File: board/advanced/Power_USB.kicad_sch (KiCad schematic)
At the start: 19 parts, among them J2 Jack-DC, J3 USB_C_Receptacle_USB2.0_16P, Q1 DMP6050SSD, SW2 SW_Reset, U4 STUSB4500QTR

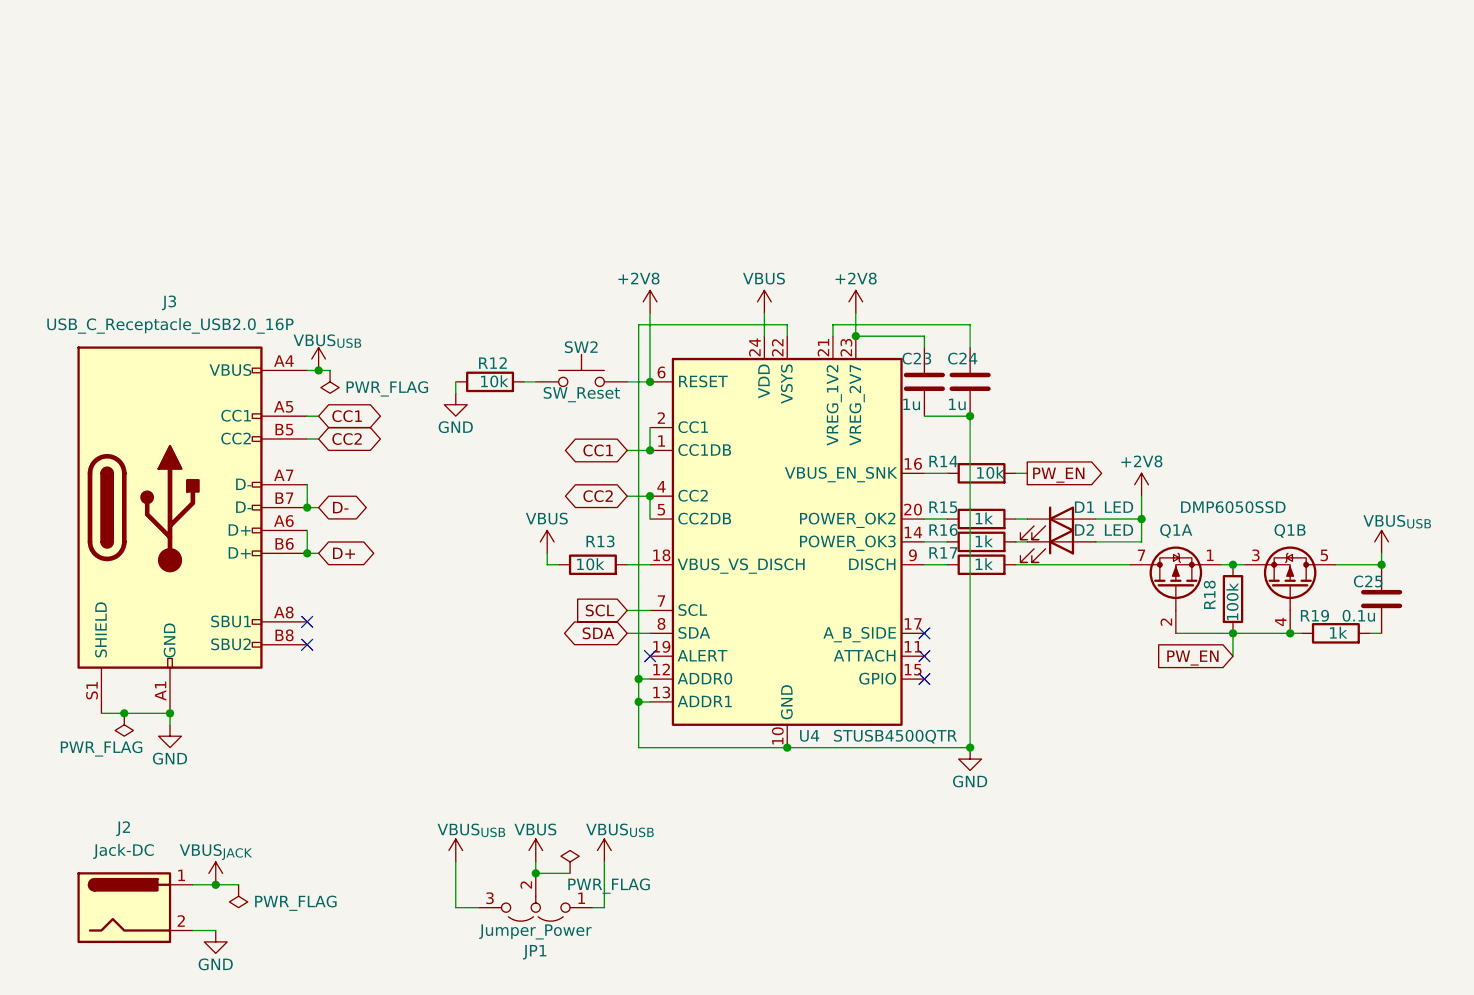
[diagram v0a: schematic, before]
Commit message: put footprints and change schematics
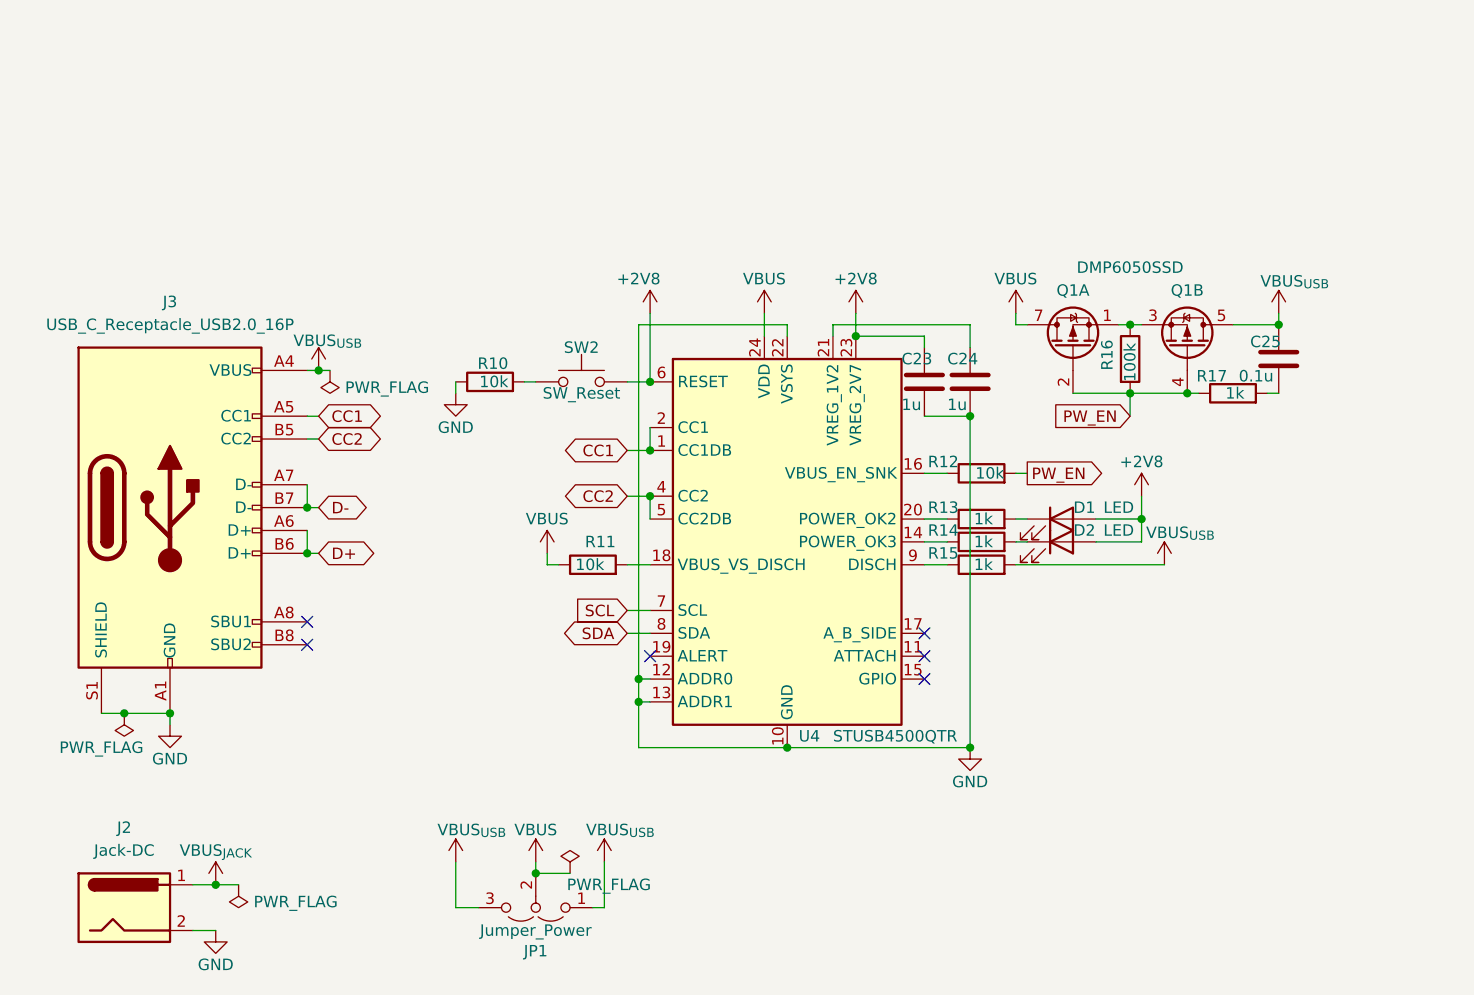
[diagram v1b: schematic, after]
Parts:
- J3: footprint Connector_USB:USB_C_Receptacle_GCT_USB4085 -> NELTRON_5077CR-16SMC2-BK-TR:NELTRON_5077CR-16SMC2-BK-TR
- R10: renamed from R12; footprint Resistor_SMD:R_0603_1608Metric -> Resistor_SMD:R_0402_1005Metric
- R11: renamed from R13; footprint Resistor_SMD:R_0603_1608Metric -> Resistor_SMD:R_0402_1005Metric
- R12: renamed from R14; footprint Resistor_SMD:R_0603_1608Metric -> Resistor_SMD:R_0402_1005Metric
- R13: renamed from R15; footprint Resistor_SMD:R_0603_1608Metric -> Resistor_SMD:R_0402_1005Metric
- R14: renamed from R16; footprint Resistor_SMD:R_0603_1608Metric -> Resistor_SMD:R_0402_1005Metric
- R15: renamed from R17; footprint Resistor_SMD:R_0603_1608Metric -> Resistor_SMD:R_0402_1005Metric
- R16: renamed from R18; footprint Resistor_SMD:R_0603_1608Metric -> Resistor_SMD:R_0402_1005Metric
- R17: renamed from R19; footprint Resistor_SMD:R_0603_1608Metric -> Resistor_SMD:R_0402_1005Metric
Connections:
- net VBUS: now also Q1.7 (D1), Q1.8 (D1)
- net VBUS_{USB}: now also R15.2
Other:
- moved on the sheet: C25, Q1A, Q1B, R16, R17

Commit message: change schematics and complete wiring
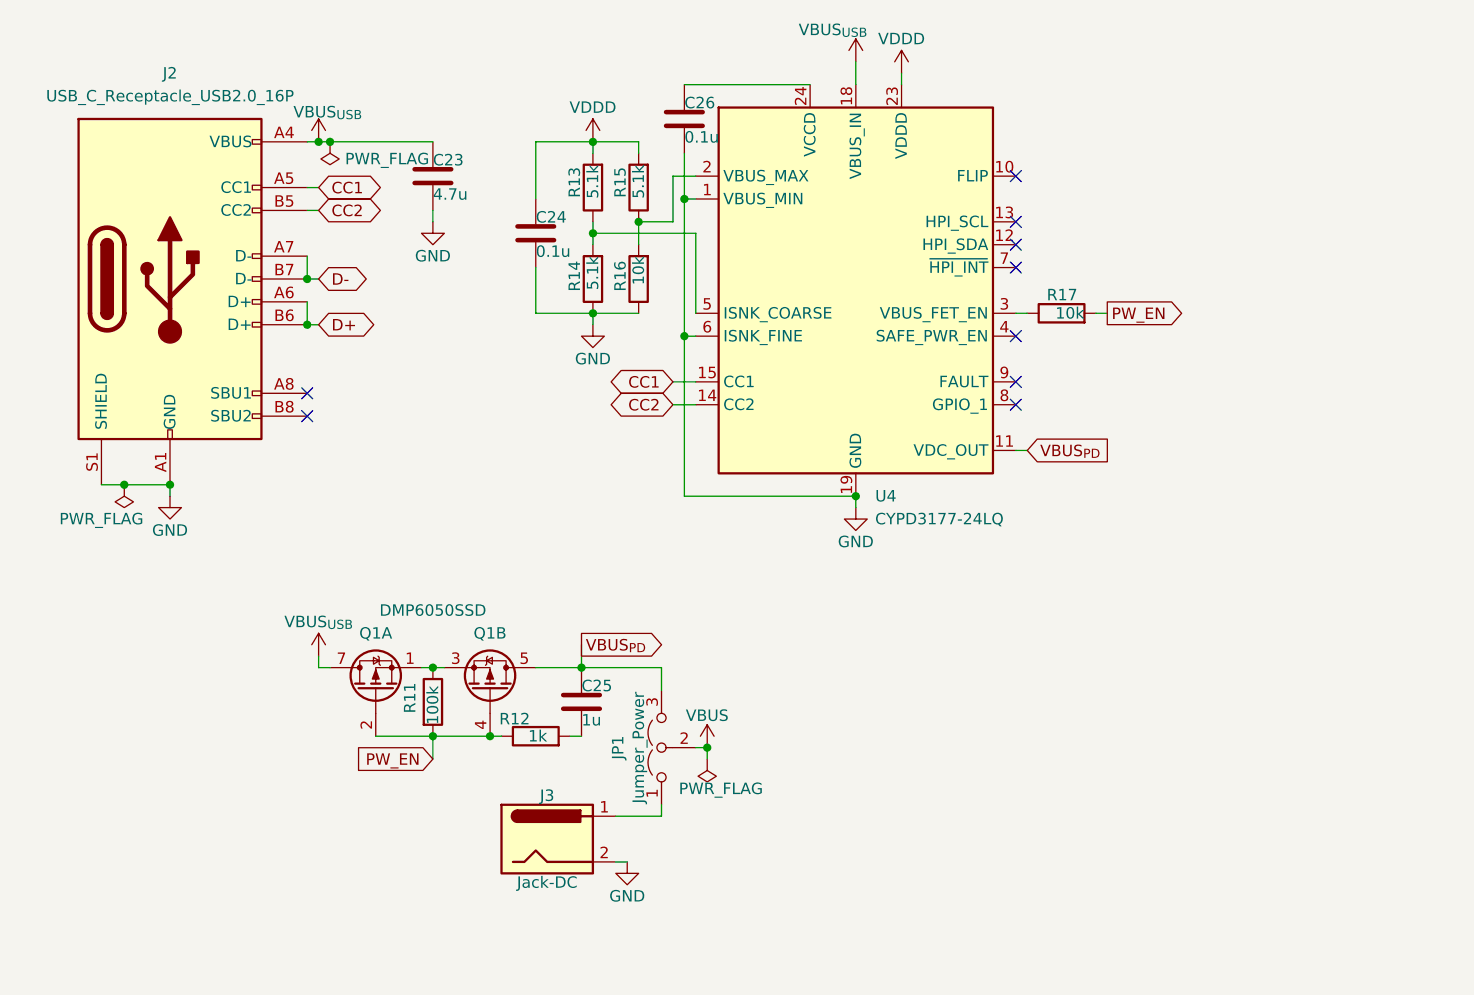
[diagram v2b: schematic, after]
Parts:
- removed D1, D2: LED, LED_SMD:LED_0603_1608Metric, symbol Device:LED
- removed R10, R11: 10k, Resistor_SMD:R_0402_1005Metric, symbol Device:R
- removed SW2: SW_Reset, SW_SKRPACE010:SW_SKRPACE010, symbol Switch:SW_Push
- removed U4: STUSB4500QTR, Package_DFN_QFN:QFN-24-1EP_4x4mm_P0.5mm_EP2.7x2.7mm, symbol Interface_USB:STUSB4500QTR
- added C26: 0.1u, C_0402_1005Metric_small_pads:C_0402_1005Metric_small_pads, symbol Device:C
- added R16: 10k, C_0402_1005Metric_small_pads:C_0402_1005Metric_small_pads, symbol Device:R
- added U4: CYPD3177-24LQ, Package_DFN_QFN:QFN-24-1EP_4x4mm_P0.5mm_EP2.75x2.75mm, symbol Interface_USB:CYPD3177-24LQ
- C23: value 1u -> 4.7u; footprint Capacitor_SMD:C_0201_0603Metric -> C_0402_1005Metric_small_pads:C_0402_1005Metric_small_pads
- C24: value 1u -> 0.1u; footprint Capacitor_SMD:C_0201_0603Metric -> C_0402_1005Metric_small_pads:C_0402_1005Metric_small_pads
- C25: value 0.1u -> 1u; footprint Capacitor_SMD:C_0201_0603Metric -> C_0402_1005Metric_small_pads:C_0402_1005Metric_small_pads
- R11: renamed from R16; footprint Resistor_SMD:R_0402_1005Metric -> C_0402_1005Metric_small_pads:C_0402_1005Metric_small_pads
- R12: renamed from R17; footprint Resistor_SMD:R_0402_1005Metric -> C_0402_1005Metric_small_pads:C_0402_1005Metric_small_pads
- R13, R14, R15: value 1k -> 5.1k; footprint Resistor_SMD:R_0402_1005Metric -> C_0402_1005Metric_small_pads:C_0402_1005Metric_small_pads
- R17: renamed from R12; footprint Resistor_SMD:R_0402_1005Metric -> C_0402_1005Metric_small_pads:C_0402_1005Metric_small_pads
- renumbered J3 to J2, J2 to J3
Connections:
- net +2V8 is gone; now on net VBUS_{USB}: C23.1
- net CC1: now also U4.15 (CC1)
- net CC2: now also U4.14 (CC2)
- net GND: now also R14.1, C26.2, R16.1, U4.1 (VBUS_MIN), U4.19 (GND), U4.22 (GND), U4.25 (GND), U4.6 (ISNK_FINE); no longer J2.A12 (GND), J2.B12 (GND)
- net VBUS: no longer Q1.7 (D1), Q1.8 (D1)
- net VBUS_{USB}: now also Q1.7 (D1), Q1.8 (D1), U4.18 (VBUS_IN); no longer C25.1, J2.A9 (VBUS), J2.B9 (VBUS), JP1.1 (A), JP1.3 (B), Q1.5 (D2), Q1.6 (D2), R15.2
- net at R17.1: now also U4.3 (VBUS_FET_EN)
- net at R14.2: now also R13.1, U4.5 (ISNK_COARSE)
- net VDDD: now reaches C24.1
- net VDDD: now also R13.2, R15.2, U4.23 (VDDD)
- net at R15.1: now also R16.2, U4.2 (VBUS_MAX)
- net VBUS_{JACK}: no longer names the net of J3.1
- net VBUS_{JACK}: now also JP1.1 (A)
- new net: C26.1, U4.24 (VCCD)
- new net VBUS_{PD}: C25.1, JP1.3 (B), Q1.5 (D2), Q1.6 (D2), U4.11 (VDC_OUT)
- no-connect marks 6 -> 9
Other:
- moved on the sheet: C23, C25, J2, J3, JP1, Q1A, Q1B, R11, R12, R17

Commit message: add LTB example and more
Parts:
- C23: Mouser Part Number (none) -> 81-GRM15D81C475ME15J; Mouser Price/Stock (none) -> https://www.mouser.jp/ProductDetail/Murata-Electronics/GRM1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
- C24, C26: Mouser Part Number (none) -> 81-GRM15R61A104KA01J; Mouser Price/Stock (none) -> https://www.mouser.jp/ProductDetail/Murata-Electronics/GRM1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
- C25: Mouser Part Number (none) -> 81-GRM155C81C105KE1D; Mouser Price/Stock (none) -> https://www.mouser.jp/ProductDetail/Murata-Electronics/GRM1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
- Q1: Mouser Part Number (none) -> 621-DMP6050SSD-13; Mouser Price/Stock (none) -> https://www.mouser.jp/ProductDetail/Diodes-Incorporated/DMP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
- R11: Mouser Part Number (none) -> 667-ERJ-2RKF1003X; Mouser Price/Stock (none) -> https://www.mouser.jp/ProductDetail/Panasonic/ERJ-2RKF1003X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
- R12: Mouser Part Number (none) -> 667-ERJ-2GEJ102X; Mouser Price/Stock (none) -> https://www.mouser.jp/ProductDetail/Panasonic/ERJ-2GEJ102X?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
- R13, R14, R15: value 5.1k -> 4.7k; Mouser Part Number (none) -> 667-ERJ-2RKF4701X; Mouser Price/Stock (none) -> https://www.mouser.jp/ProductDetail/Panasonic/ERJ-2RKF4701X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
- R16, R17: Mouser Part Number (none) -> 667-ERJ-2GEJ103X; Mouser Price/Stock (none) -> https://www.mouser.jp/ProductDetail/Panasonic/ERJ-2GEJ103X?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
- U4: Mouser Part Number (none) -> 727-CYPD3177-24LQXQ; Mouser Price/Stock (none) -> https://www.mouser.jp/ProductDetail/Infineon-Technologies/C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
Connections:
- net GND: now also R15.1; no longer R16.1
- net VDDD: now also R16.2; no longer R15.2
- new net: R15.2, R16.1, U4.2 (VBUS_MAX)
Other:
- moved on the sheet: R15, R16
